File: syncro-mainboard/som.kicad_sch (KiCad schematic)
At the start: 11 parts, among them U1 MYC-YF135

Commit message: Syncro mainboard rev 2
* Migrate I2C to I2C5 on SOM pins 132/133
* Use correctly reversed LED footprint
* Use updated rear graphics
* Set SOM to be assembled at JLC
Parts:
- U1: LCSC (none) -> C9900196745
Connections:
- net I2C_SCL: now also U1.133 (PH13/LTDC_G2); no longer U1.93 (PH3/I2C3_SCL)
- net I2C_SDA: now also U1.132 (PF3/LTDC_G3); no longer U1.94 (PH7/I2C3_SDA)
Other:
- title: STM32MP13 SOM -> Syncro FFB Interceptor
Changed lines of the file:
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@@
 	(paper "USLetter")
 	(title_block
-		(title "STM32MP13 SOM")
-		(date "2026-08-25")
-		(rev "1")
+		(title "Syncro FFB Interceptor")
+		(date "2026-10-23")
+		(rev "2")
 		(company "Deadband Inc.")
 	)
+	(text_box "Revision 2 Note:\n * Moved I2C to I2C5 pins 132/133 due to I2C3 conflict with internal EEPROM"
+		(exclude_from_sim no)
+		(at 153.67 142.8132 0)
+		(size 48.26 8.3168)
+		(margins 0.9525 0.9525 0.9525 0.9525)
+		(stroke
+			(width 0)
+			(type solid)
+		)
+		(fill
+			(type none)
+		)
+		(effects
+			(font
+				(size 1.27 1.27)
+				(italic yes)
+			)
+			(justify left top)
+		)
+	)
 	(junction
 		(at 92.71 36.83)
@@
 	)
 	(no_connect
-		(at 148.59 154.94)
-	)
-	(no_connect
 		(at 22.86 168.91)
 	)
@@
 	)
 	(no_connect
-		(at 148.59 157.48)
-	)
-	(no_connect
 		(at 97.79 154.94)
 	)
@@
 	)
 	(no_connect
+		(at 234.95 49.53)
+	)
+	(no_connect
 		(at 83.82 135.89)
 	)
@@
 	)
 	(no_connect
+		(at 234.95 46.99)
+	)
+	(no_connect
 		(at 22.86 138.43)
 	)
@@
 	(wire
 		(pts
+			(xy 148.59 154.94) (xy 153.67 154.94)
+		)
+		(stroke
+			(width 0)
+			(type default)
+		)
+	)
+	(wire
+		(pts
 			(xy 175.26 44.45) (xy 180.34 44.45)
 		)
@@
 	(wire
 		(pts
+			(xy 148.59 157.48) (xy 153.67 157.48)
+		)
+		(stroke
+			(width 0)
+			(type default)
+		)
+	)
+	(wire
+		(pts
 			(xy 234.95 62.23) (xy 240.03 62.23)
 		)
@@
 	(wire
 		(pts
-			(xy 234.95 46.99) (xy 240.03 46.99)
-		)
-		(stroke
-			(width 0)
-			(type default)
-		)
-	)
-	(wire
-		(pts
 			(xy 234.95 69.85) (xy 240.03 69.85)
 		)
@@
 		(pts
 			(xy 175.26 34.29) (xy 180.34 34.29)
-		)
-		(stroke
-			(width 0)
-			(type default)
-		)
-	)
-	(wire
-		(pts
-			(xy 234.95 49.53) (xy 240.03 49.53)
 		)
 		(stroke
@@
 		)
 	)
-	(hierarchical_label "I2C_SDA"
-		(shape input)
-		(at 240.03 49.53 0)
-		(effects
-			(font
-				(size 1.27 1.27)
-			)
-			(justify left)
-		)
-	)
-	(hierarchical_label "I2C_SCL"
-		(shape input)
-		(at 240.03 46.99 0)
-		(effects
-			(font
-				(size 1.27 1.27)
-			)
-			(justify left)
-		)
-	)
 	(hierarchical_label "SPI_SDI"
 		(shape input)
@@
 		)
 	)
+	(hierarchical_label "I2C_SCL"
+		(shape input)
+		(at 153.67 157.48 0)
+		(effects
+			(font
+				(size 1.27 1.27)
+			)
+			(justify left)
+		)
+	)
 	(hierarchical_label "SOM_USB2_D_P"
 		(shape bidirectional)
@@
 		(shape input)
 		(at 180.34 44.45 0)
+		(effects
+			(font
+				(size 1.27 1.27)
+			)
+			(justify left)
+		)
+	)
+	(hierarchical_label "I2C_SDA"
+		(shape input)
+		(at 153.67 154.94 0)
 		(effects
 			(font
@@
 			(hide yes)
 			(show_name no)
+			(do_not_autoplace no)
+			(effects
+				(font
+					(size 1.27 1.27)
+				)
+			)
+		)
+		(property "LCSC" "C9900196745"
+			(at 160.02 48.26 0)
+			(hide yes)
+			(show_name no)

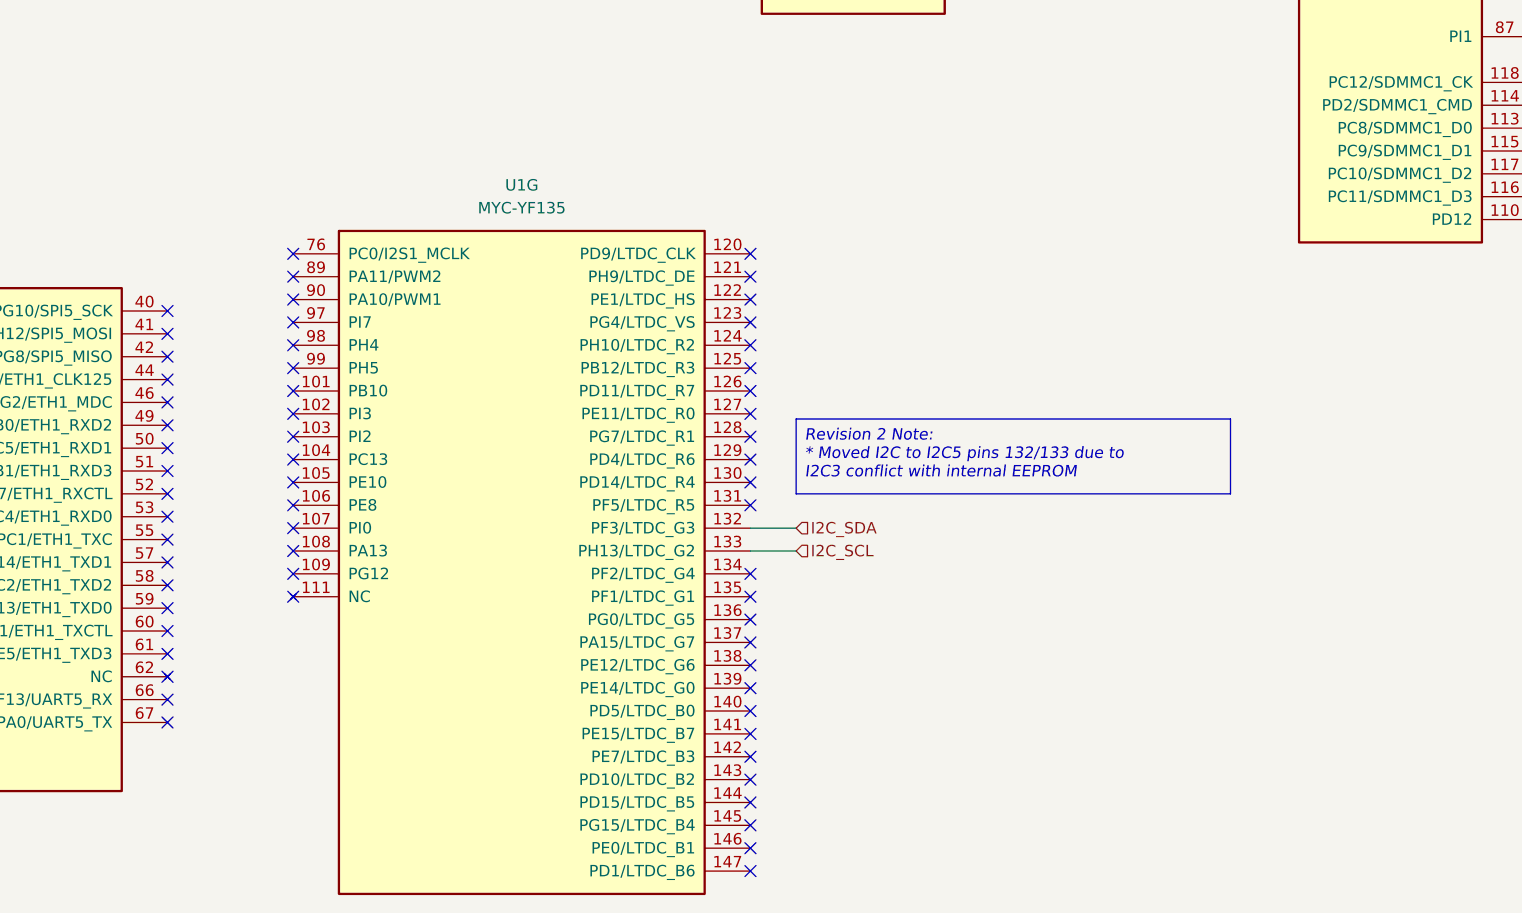
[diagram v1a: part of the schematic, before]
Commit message: Syncro mainboard rev 3
* Add XL-1615 accent RGB LEDs D16-D18 on TIM8
* Add R48-R56 next to the LEDs and rework their shared +3.3V feed
* Add In2 GND return plane under the USB-C connector for TP5/TP6
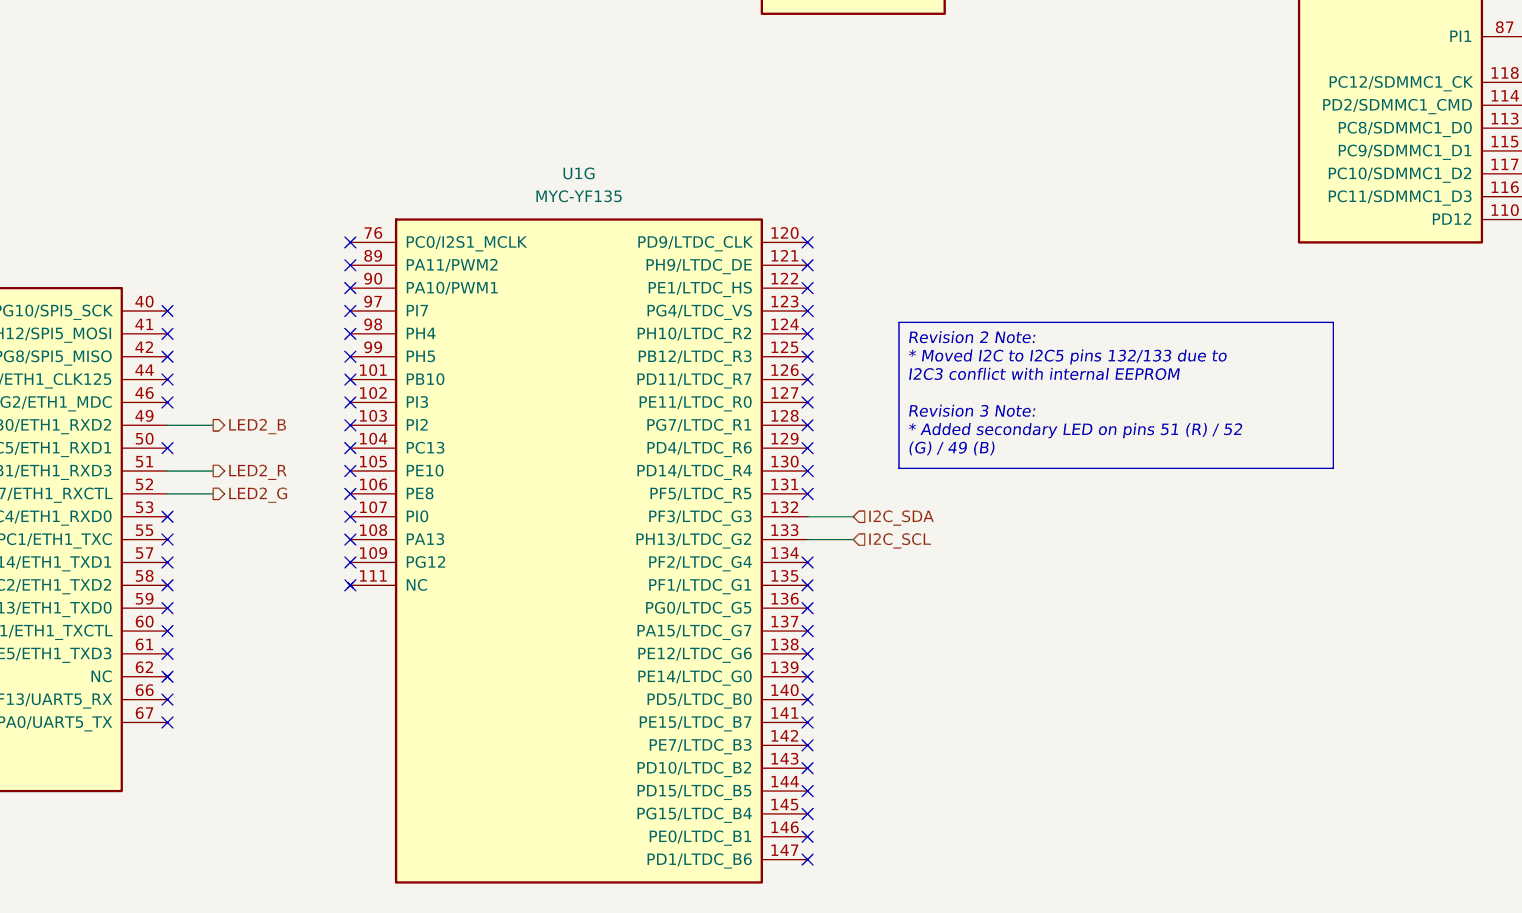
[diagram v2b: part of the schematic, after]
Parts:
- U1: LCSC C9900196745 -> (none); MPN (none) -> MYC-YF135F-256N256D-100-I; Manufacturer (none) -> MYIR
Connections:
- net LED2_B: now reaches U1.49 (PB0/ETH1_RXD2)
- net LED2_R: now reaches U1.51 (PB1/ETH1_RXD3)
- net LED2_G: now reaches U1.52 (PA7/ETH1_RXCTL)
- no-connect marks 84 -> 81
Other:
- moved on the sheet: U1G
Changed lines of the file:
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@@
 		(company "Deadband Inc.")
 	)
-	(text_box "Revision 2 Note:\n * Moved I2C to I2C5 pins 132/133 due to I2C3 conflict with internal EEPROM"
+	(text_box "Revision 2 Note:\n * Moved I2C to I2C5 pins 132/133 due to I2C3 conflict with internal EEPROM\n\nRevision 3 Note:\n * Added secondary LED on pins 51 (R) / 52 (G) / 49 (B)"
 		(exclude_from_sim no)
-		(at 153.67 142.8132 0)
-		(size 48.26 8.3168)
+		(at 165.1 132.08 0)
+		(size 48.26 16.2161)
 		(margins 0.9525 0.9525 0.9525 0.9525)
 		(stroke
@@
 	)
 	(no_connect
-		(at 148.59 185.42)
+		(at 154.94 184.15)
 	)
 	(no_connect
-		(at 148.59 172.72)
+		(at 154.94 171.45)
 	)
 	(no_connect
-		(at 148.59 127)
+		(at 154.94 125.73)
 	)
 	(no_connect
@@
 	)
 	(no_connect
-		(at 83.82 151.13)
+		(at 104.14 140.97)
 	)
 	(no_connect
-		(at 97.79 142.24)
-	)
-	(no_connect
-		(at 148.59 167.64)
+		(at 154.94 166.37)
 	)
 	(no_connect
@@
 	)
 	(no_connect
-		(at 148.59 139.7)
+		(at 154.94 138.43)
 	)
 	(no_connect
-		(at 148.59 134.62)
+		(at 154.94 133.35)
 	)
 	(no_connect
-		(at 97.79 149.86)
+		(at 104.14 148.59)
 	)
 	(no_connect
-		(at 148.59 149.86)
+		(at 154.94 148.59)
 	)
 	(no_connect
@@
 	)
 	(no_connect
-		(at 97.79 139.7)
+		(at 104.14 138.43)
 	)
 	(no_connect
@@
 	)
 	(no_connect
-		(at 148.59 142.24)
+		(at 154.94 140.97)
 	)
 	(no_connect
-		(at 97.79 154.94)
+		(at 104.14 153.67)
 	)
 	(no_connect
@@
 	)
 	(no_connect
-		(at 148.59 152.4)
+		(at 154.94 151.13)
 	)
 	(no_connect
@@
 	)
 	(no_connect
-		(at 97.79 132.08)
+		(at 104.14 130.81)
 	)
 	(no_connect
@@
 	)
 	(no_connect
-		(at 148.59 124.46)
+		(at 154.94 123.19)
 	)
 	(no_connect
@@
 	)
 	(no_connect
-		(at 148.59 129.54)
+		(at 154.94 128.27)
 	)
 	(no_connect
@@
 	)
 	(no_connect
-		(at 97.79 144.78)
+		(at 104.14 143.51)
 	)
 	(no_connect
@@
 	)
 	(no_connect
-		(at 148.59 175.26)
+		(at 154.94 173.99)
 	)
 	(no_connect
-		(at 148.59 193.04)
+		(at 154.94 191.77)
 	)
 	(no_connect
@@
 	)
 	(no_connect
-		(at 148.59 162.56)
+		(at 154.94 161.29)
 	)
 	(no_connect
-		(at 83.82 143.51)
-	)
-	(no_connect
-		(at 97.79 137.16)
+		(at 104.14 135.89)
 	)
 	(no_connect
@@
 	)
 	(no_connect
-		(at 97.79 162.56)
+		(at 104.14 161.29)
 	)
 	(no_connect
@@
 	)
 	(no_connect
-		(at 148.59 132.08)
+		(at 154.94 130.81)
 	)
 	(no_connect
-		(at 148.59 177.8)
+		(at 154.94 176.53)
 	)
 	(no_connect
@@
 	)
 	(no_connect
-		(at 148.59 147.32)
+		(at 154.94 146.05)
 	)
 	(no_connect
@@
 	)
 	(no_connect
-		(at 83.82 148.59)
-	)
-	(no_connect
-		(at 97.79 127)
+		(at 104.14 125.73)
 	)
 	(no_connect
-		(at 97.79 157.48)
+		(at 104.14 156.21)
 	)
 	(no_connect
-		(at 148.59 187.96)
+		(at 154.94 186.69)
 	)
 	(no_connect
-		(at 148.59 160.02)
+		(at 154.94 158.75)
 	)
 	(no_connect
-		(at 148.59 137.16)
+		(at 154.94 135.89)
 	)
 	(no_connect
@@
 	)
 	(no_connect
-		(at 97.79 152.4)
+		(at 104.14 151.13)
 	)
 	(no_connect
-		(at 148.59 170.18)
+		(at 154.94 168.91)
 	)
 	(no_connect
@@
 	)
 	(no_connect
-		(at 97.79 160.02)
+		(at 104.14 158.75)
 	)
 	(no_connect
@@
 	)
 	(no_connect
-		(at 148.59 190.5)
+		(at 154.94 189.23)
 	)
 	(no_connect
-		(at 97.79 129.54)
+		(at 104.14 128.27)
 	)
 	(no_connect
-		(at 148.59 180.34)
+		(at 154.94 179.07)
 	)
 	(no_connect
@@
 	)
 	(no_connect
-		(at 148.59 182.88)
+		(at 154.94 181.61)
 	)
 	(no_connect
@@
 	)
 	(no_connect
-		(at 97.79 147.32)
+		(at 104.14 146.05)
 	)
 	(no_connect
@@
 	)
 	(no_connect
-		(at 148.59 144.78)
+		(at 154.94 143.51)
 	)
 	(no_connect
@@
 	)
 	(no_connect
-		(at 97.79 134.62)
+		(at 104.14 133.35)
 	)
 	(no_connect
-		(at 97.79 124.46)
+		(at 104.14 123.19)
 	)
 	(no_connect
@@
 	)
 	(no_connect
-		(at 148.59 165.1)
+		(at 154.94 163.83)
 	)
 	(no_connect
@@
 	(wire
 		(pts
+			(xy 83.82 151.13) (xy 88.9 151.13)
+		)
+		(stroke
+			(width 0)
+			(type default)
+		)
+	)
+	(wire
+		(pts
 			(xy 100.33 77.47) (xy 110.49 77.47)
 		)
@@
 	(wire
 		(pts
-			(xy 148.59 154.94) (xy 153.67 154.94)
+			(xy 154.94 153.67) (xy 160.02 153.67)
 		)
 		(stroke
@@
 	(wire
 		(pts
-			(xy 148.59 157.48) (xy 153.67 157.48)
+			(xy 154.94 156.21) (xy 160.02 156.21)
 		)
 		(stroke
@@
 	(wire
 		(pts
+			(xy 83.82 143.51) (xy 88.9 143.51)
+		)
+		(stroke
+			(width 0)
+			(type default)
+		)
+	)
+	(wire
+		(pts
 			(xy 175.26 52.07) (xy 180.34 52.07)
 		)
@@
 	(wire
 		(pts
+			(xy 83.82 148.59) (xy 88.9 148.59)
+		)
+		(stroke
+			(width 0)
+			(type default)
+		)
+	)
+	(wire
+		(pts
 			(xy 175.26 49.53) (xy 180.34 49.53)
 		)
@@
 		)
 	)
+	(hierarchical_label "LED2_B"
+		(shape output)
+		(at 88.9 143.51 0)
+		(effects
+			(font
+				(size 1.27 1.27)
+			)
+			(justify left)
+		)
+	)
 	(hierarchical_label "SPI_SDO"
 		(shape input)
@@
 		)
 	)
+	(hierarchical_label "LED2_R"
+		(shape output)
+		(at 88.9 148.59 0)
+		(effects
+			(font
+				(size 1.27 1.27)
+			)
+			(justify left)
+		)
+	)
 	(hierarchical_label "SD_D3"
 		(shape bidirectional)
@@
 		)
 	)
+	(hierarchical_label "LED2_G"
+		(shape output)
+		(at 88.9 151.13 0)
+		(effects
+			(font
+				(size 1.27 1.27)
+			)
+			(justify left)
+		)
+	)
 	(hierarchical_label "SPI_SDI"
 		(shape input)
@@
 	(hierarchical_label "I2C_SCL"
 		(shape input)
-		(at 153.67 157.48 0)
+		(at 160.02 156.21 0)
 		(effects
 			(font
@@
 	(hierarchical_label "I2C_SDA"
 		(shape input)
-		(at 153.67 154.94 0)
+		(at 160.02 153.67 0)
 		(effects
 			(font
@@
 			)
 		)
-		(property "LCSC" "C9900196745"
+		(property "LCSC" ""
+			(at 160.02 48.26 0)
+			(hide yes)
+			(show_name no)
+			(do_not_autoplace no)
+			(effects
+				(font
+					(size 1.27 1.27)
+				)
+			)
+		)
+		(property "MPN" "MYC-YF135F-256N256D-100-I"
+			(at 160.02 48.26 0)
+			(hide yes)
+			(show_name no)
+			(do_not_autoplace no)
+			(effects
+				(font
+					(size 1.27 1.27)
+				)
+			)
+		)
+		(property "Manufacturer" "MYIR"
 			(at 160.02 48.26 0)
 			(hide yes)
@@
 	(symbol
 		(lib_id "dbl-ic:MYC-YF135")
-		(at 123.19 157.48 0)
+		(at 129.54 156.21 0)
 		(unit 7)
 		(body_style 1)
@@
 		(dnp no)
 		(property "Reference" "U1"
-			(at 123.19 116.84 0)
+			(at 129.54 115.57 0)
 			(show_name no)
 			(do_not_autoplace no)
@@
 		)
 		(property "Value" "MYC-YF135"
-			(at 123.19 119.38 0)
+			(at 129.54 118.11 0)
 			(show_name no)
 			(do_not_autoplace no)
@@
 		)
 		(property "Footprint" "dbl-ic:MYC-YF135"
-			(at 123.19 157.48 0)
+			(at 129.54 156.21 0)
 			(hide yes)
 			(show_name no)
@@
 		)
 		(property "Datasheet" "MYC-YF13X Product Manual-1.2.pdf"
-			(at 123.19 157.48 0)
+			(at 129.54 156.21 0)
 			(hide yes)
 			(show_name no)
@@
 		)
 		(property "Description" "MYIR MYC-YF135 STM32MP135 castellated-edge SOM; 37 mm x 39 mm; 148 pads"
-			(at 123.19 157.48 0)
+			(at 129.54 156.21 0)
 			(hide yes)
 			(show_name no)
